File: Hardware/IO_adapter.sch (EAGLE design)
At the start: 23 parts, among them Y1 32Khz

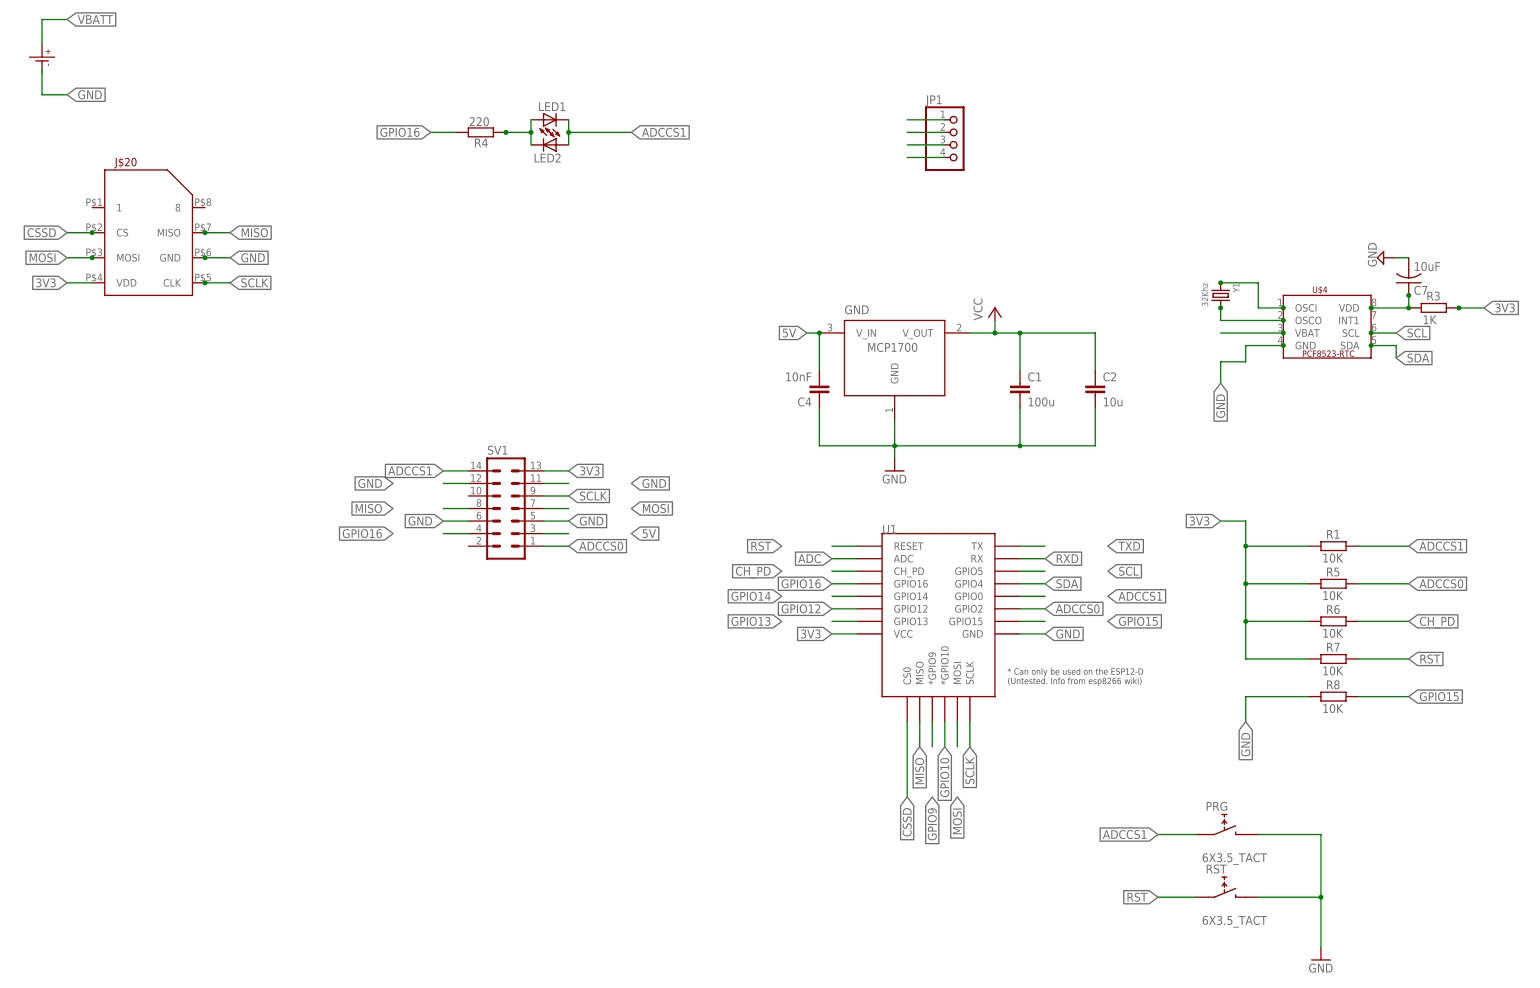
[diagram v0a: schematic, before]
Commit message: corrected sd card orientation
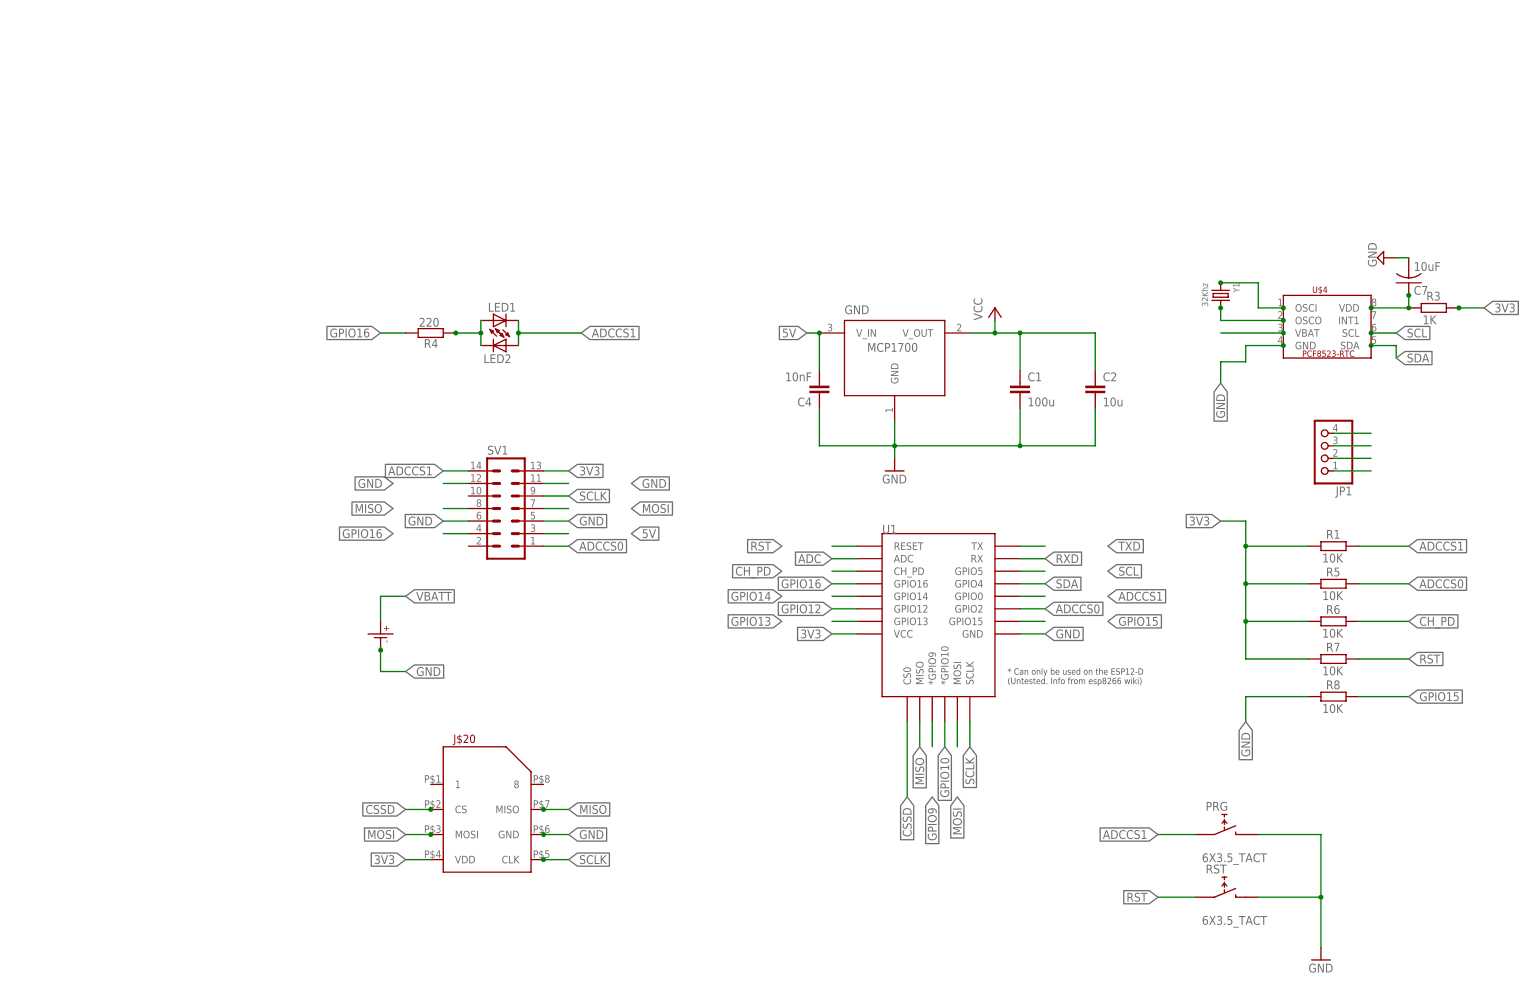
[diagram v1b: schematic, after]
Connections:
- net GND: now also U$1.P$-
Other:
- moved on the sheet: J$20, JP1, LED1, LED2, R4
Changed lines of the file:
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@@
 <part name="GND1" library="supply1" deviceset="GND" device=""/>
 <part name="JP1" library="pinhead" deviceset="PINHD-1X4" device=""/>
+<part name="FRAME1" library="frames" deviceset="DINA3_L" device=""/>
 </parts>
 <sheets>
@@
 </plain>
 <instances>
-<instance part="J$20" gate="G$1" x="5.08" y="66.04"/>
-<instance part="R4" gate="G$1" x="73.66" y="88.9" smashed="yes" rot="R180">
-<attribute name="NAME" x="75.184" y="87.6554" size="1.778" layer="95" rot="R180"/>
-<attribute name="VALUE" x="75.438" y="91.948" size="1.778" layer="96" rot="R180"/>
-</instance>
-<instance part="U$1" gate="G$1" x="-15.24" y="104.14" rot="R270"/>
+<instance part="J$20" gate="G$1" x="73.66" y="-50.8"/>
+<instance part="R4" gate="G$1" x="63.5" y="48.26" smashed="yes" rot="R180">
+<attribute name="NAME" x="65.024" y="47.0154" size="1.778" layer="95" rot="R180"/>
+<attribute name="VALUE" x="65.278" y="51.308" size="1.778" layer="96" rot="R180"/>
+</instance>
+<instance part="U$1" gate="G$1" x="53.34" y="-12.7" rot="R270"/>
 <instance part="GND" gate="G$1" x="157.48" y="38.1"/>
 <instance part="GND3" gate="1" x="157.48" y="20.32"/>
@@
 <attribute name="VALUE" x="264.414" y="50.038" size="1.778" layer="96"/>
 </instance>
-<instance part="LED1" gate="G$1" x="86.36" y="91.44" rot="R90"/>
-<instance part="LED2" gate="G$1" x="88.9" y="86.36" rot="R270"/>
+<instance part="LED1" gate="G$1" x="76.2" y="50.8" rot="R90"/>
+<instance part="LED2" gate="G$1" x="78.74" y="45.72" rot="R270"/>
 <instance part="PRG" gate="G$1" x="223.52" y="-53.34"/>
 <instance part="RST" gate="G$1" x="223.52" y="-66.04"/>
 <instance part="GND1" gate="1" x="243.84" y="-78.74"/>
-<instance part="JP1" gate="A" x="170.18" y="86.36"/>
+<instance part="JP1" gate="A" x="243.84" y="25.4" rot="R180"/>
+<instance part="FRAME1" gate="G$1" x="-10.16" y="-142.24"/>
+<instance part="FRAME1" gate="G$2" x="276.86" y="-142.24"/>
 </instances>
 <busses>
@@
 <segment>
 <pinref part="J$20" gate="G$1" pin="GND"/>
-<junction x="17.78" y="63.5"/>
-<wire x1="17.78" y1="63.5" x2="22.86" y2="63.5" width="0.1524" layer="91"/>
-<label x="22.86" y="63.5" size="1.778" layer="91" xref="yes"/>
+<junction x="86.36" y="-53.34"/>
+<wire x1="86.36" y1="-53.34" x2="91.44" y2="-53.34" width="0.1524" layer="91"/>
+<label x="91.44" y="-53.34" size="1.778" layer="91" xref="yes"/>
 </segment>
 <segment>
@@
 </segment>
 <segment>
-<wire x1="-15.24" y1="101.6" x2="-15.24" y2="96.52" width="0.1524" layer="91"/>
-<wire x1="-15.24" y1="96.52" x2="-10.16" y2="96.52" width="0.1524" layer="91"/>
-<label x="-10.16" y="96.52" size="1.778" layer="91" font="vector" xref="yes"/>
+<wire x1="53.34" y1="-15.24" x2="53.34" y2="-16.002" width="0.1524" layer="91"/>
+<wire x1="53.34" y1="-16.002" x2="53.34" y2="-20.32" width="0.1524" layer="91"/>
+<wire x1="53.34" y1="-20.32" x2="58.42" y2="-20.32" width="0.1524" layer="91"/>
+<label x="58.42" y="-20.32" size="1.778" layer="91" font="vector" xref="yes"/>
+<pinref part="U$1" gate="G$1" pin="P$-"/>
+<junction x="53.34" y="-16.002"/>
 </segment>
 <segment>
@@
 <segment>
 <pinref part="JP1" gate="A" pin="4"/>
-<wire x1="167.64" y1="83.82" x2="160.02" y2="83.82" width="0.1524" layer="91"/>
+<wire x1="246.38" y1="27.94" x2="254" y2="27.94" width="0.1524" layer="91"/>
 </segment>
 </net>
@@
 <segment>
 <pinref part="J$20" gate="G$1" pin="MISO"/>
-<junction x="17.78" y="68.58"/>
-<wire x1="17.78" y1="68.58" x2="22.86" y2="68.58" width="0.1524" layer="91"/>
-<label x="22.86" y="68.58" size="1.778" layer="91" xref="yes"/>
+<junction x="86.36" y="-48.26"/>
+<wire x1="86.36" y1="-48.26" x2="91.44" y2="-48.26" width="0.1524" layer="91"/>
+<label x="91.44" y="-48.26" size="1.778" layer="91" xref="yes"/>
 </segment>
 <segment>
@@
 <segment>
 <pinref part="J$20" gate="G$1" pin="MOSI"/>
-<junction x="-5.08" y="63.5"/>
-<wire x1="-5.08" y1="63.5" x2="-10.16" y2="63.5" width="0.1524" layer="91"/>
-<label x="-10.16" y="63.5" size="1.778" layer="91" rot="R180" xref="yes"/>
+<junction x="63.5" y="-53.34"/>
+<wire x1="63.5" y1="-53.34" x2="58.42" y2="-53.34" width="0.1524" layer="91"/>
+<label x="58.42" y="-53.34" size="1.778" layer="91" rot="R180" xref="yes"/>
 </segment>
 <segment>
@@
 <segment>
 <pinref part="J$20" gate="G$1" pin="CLK"/>
-<junction x="17.78" y="58.42"/>
-<wire x1="17.78" y1="58.42" x2="22.86" y2="58.42" width="0.1524" layer="91"/>
-<label x="22.86" y="58.42" size="1.778" layer="91" xref="yes"/>
+<junction x="86.36" y="-58.42"/>
+<wire x1="86.36" y1="-58.42" x2="91.44" y2="-58.42" width="0.1524" layer="91"/>
+<label x="91.44" y="-58.42" size="1.778" layer="91" xref="yes"/>
 </segment>
 <segment>
@@
 <segment>
 <pinref part="J$20" gate="G$1" pin="VDD"/>
-<wire x1="-5.08" y1="58.42" x2="-10.16" y2="58.42" width="0.1524" layer="91"/>
-<label x="-10.16" y="58.42" size="1.778" layer="91" rot="R180" xref="yes"/>
+<wire x1="63.5" y1="-58.42" x2="58.42" y2="-58.42" width="0.1524" layer="91"/>
+<label x="58.42" y="-58.42" size="1.778" layer="91" rot="R180" xref="yes"/>
 </segment>
 <segment>
@@
 <segment>
 <pinref part="JP1" gate="A" pin="1"/>
-<wire x1="167.64" y1="91.44" x2="160.02" y2="91.44" width="0.1524" layer="91"/>
+<wire x1="246.38" y1="20.32" x2="254" y2="20.32" width="0.1524" layer="91"/>
 </segment>
 </net>
 <net name="ADCCS1" class="0">
 <segment>
-<label x="104.14" y="88.9" size="1.778" layer="91" xref="yes"/>
+<label x="93.98" y="48.26" size="1.778" layer="91" xref="yes"/>
 <pinref part="LED1" gate="G$1" pin="C"/>
 <pinref part="LED2" gate="G$1" pin="A"/>
-<wire x1="91.44" y1="91.44" x2="91.44" y2="88.9" width="0.1524" layer="91"/>
-<wire x1="91.44" y1="88.9" x2="91.44" y2="86.36" width="0.1524" layer="91"/>
-<wire x1="104.14" y1="88.9" x2="91.44" y2="88.9" width="0.1524" layer="91"/>
-<junction x="91.44" y="88.9"/>
+<wire x1="81.28" y1="50.8" x2="81.28" y2="48.26" width="0.1524" layer="91"/>
+<wire x1="81.28" y1="48.26" x2="81.28" y2="45.72" width="0.1524" layer="91"/>
+<wire x1="93.98" y1="48.26" x2="81.28" y2="48.26" width="0.1524" layer="91"/>
+<junction x="81.28" y="48.26"/>
 </segment>
 <segment>
@@
 <segment>
 <pinref part="J$20" gate="G$1" pin="CS"/>
-<junction x="-5.08" y="68.58"/>
-<wire x1="-5.08" y1="68.58" x2="-10.16" y2="68.58" width="0.1524" layer="91"/>
-<label x="-10.16" y="68.58" size="1.778" layer="91" rot="R180" xref="yes"/>
+<junction x="63.5" y="-48.26"/>
+<wire x1="63.5" y1="-48.26" x2="58.42" y2="-48.26" width="0.1524" layer="91"/>
+<label x="58.42" y="-48.26" size="1.778" layer="91" rot="R180" xref="yes"/>
 </segment>
 <segment>
@@
 <segment>
 <pinref part="R4" gate="G$1" pin="1"/>
-<wire x1="78.74" y1="88.9" x2="83.82" y2="88.9" width="0.1524" layer="91"/>
-<junction x="78.74" y="88.9"/>
-<wire x1="83.82" y1="88.9" x2="83.82" y2="86.36" width="0.1524" layer="91"/>
+<wire x1="68.58" y1="48.26" x2="73.66" y2="48.26" width="0.1524" layer="91"/>
+<junction x="68.58" y="48.26"/>
+<wire x1="73.66" y1="48.26" x2="73.66" y2="45.72" width="0.1524" layer="91"/>
 <pinref part="LED2" gate="G$1" pin="C"/>
 <pinref part="LED1" gate="G$1" pin="A"/>
-<wire x1="83.82" y1="88.9" x2="83.82" y2="91.44" width="0.1524" layer="91"/>
-<junction x="83.82" y="88.9"/>
+<wire x1="73.66" y1="48.26" x2="73.66" y2="50.8" width="0.1524" layer="91"/>
+<junction x="73.66" y="48.26"/>
 </segment>
 </net>
@@
 <segment>
 <pinref part="R4" gate="G$1" pin="2"/>
-<wire x1="68.58" y1="88.9" x2="63.5" y2="88.9" width="0.1524" layer="91"/>
-<label x="63.5" y="88.9" size="1.778" layer="91" rot="R180" xref="yes"/>
+<wire x1="58.42" y1="48.26" x2="53.34" y2="48.26" width="0.1524" layer="91"/>
+<label x="53.34" y="48.26" size="1.778" layer="91" rot="R180" xref="yes"/>
 </segment>
 <segment>
@@
 <segment>
 <pinref part="U$1" gate="G$1" pin="P$+"/>
-<wire x1="-15.24" y1="106.68" x2="-15.24" y2="111.76" width="0.1524" layer="91"/>
-<wire x1="-15.24" y1="111.76" x2="-10.16" y2="111.76" width="0.1524" layer="91"/>
-<label x="-10.16" y="111.76" size="1.778" layer="91" font="vector" xref="yes"/>
+<wire x1="53.34" y1="-10.16" x2="53.34" y2="-5.08" width="0.1524" layer="91"/>
+<wire x1="53.34" y1="-5.08" x2="58.42" y2="-5.08" width="0.1524" layer="91"/>
+<label x="58.42" y="-5.08" size="1.778" layer="91" font="vector" xref="yes"/>
 </segment>
 <segment>
@@
 <segment>
 <pinref part="JP1" gate="A" pin="3"/>
-<wire x1="167.64" y1="86.36" x2="160.02" y2="86.36" width="0.1524" layer="91"/>
+<wire x1="246.38" y1="25.4" x2="254" y2="25.4" width="0.1524" layer="91"/>
 </segment>
 </net>
@@
 <segment>
 <pinref part="JP1" gate="A" pin="2"/>
-<wire x1="167.64" y1="88.9" x2="160.02" y2="88.9" width="0.1524" layer="91"/>
-</segment>
-</net>
+<wire x1="246.38" y1="22.86" x2="254" y2="22.86" width="0.1524" layer="91"/>
+</segment>
+</net>
